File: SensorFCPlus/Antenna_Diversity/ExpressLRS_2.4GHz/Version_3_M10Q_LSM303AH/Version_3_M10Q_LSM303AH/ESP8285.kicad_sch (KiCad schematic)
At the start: 24 parts, among them U5 ESP8285H16, Y1 26MHz

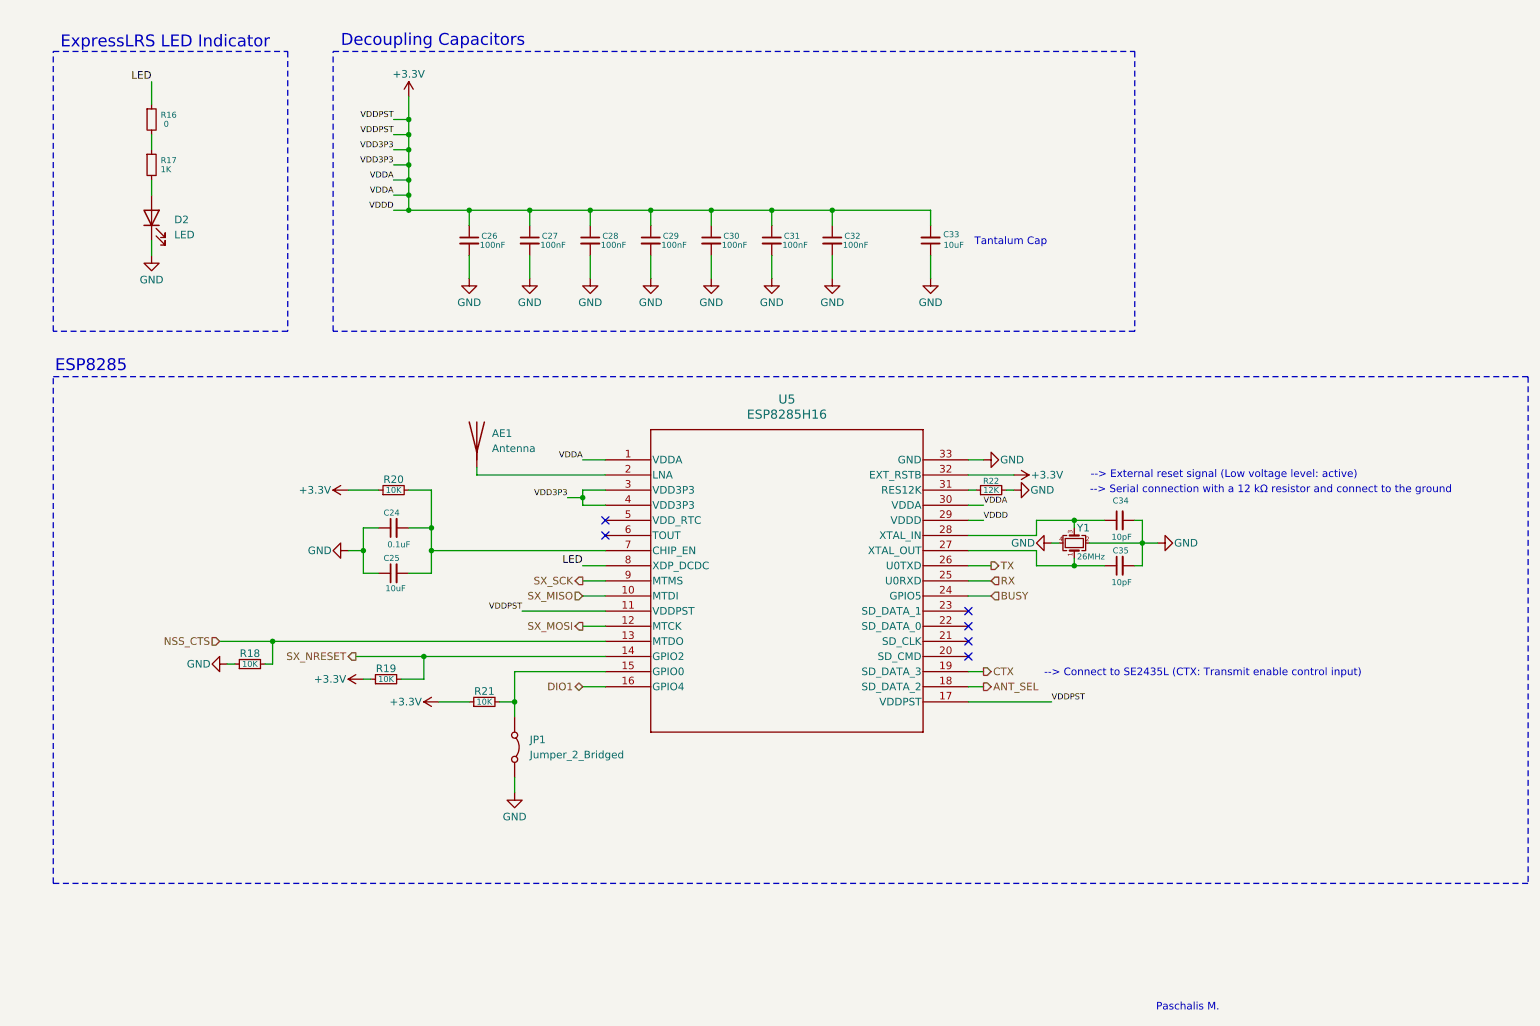
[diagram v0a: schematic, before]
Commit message: Update KiCad files for ExpressLRS modules
- Modified:
  - 2.4GHz Version 3 (M10Q LSM303AH) project and schematic files
  - 900MHz Version 3 (M10Q LSM303AH) schematic files for ESP8285 and SE2435L

- Added:
  - 2.4GHz Version 3 schematics: ESP8285, SE2431, SE2431L, SX1280
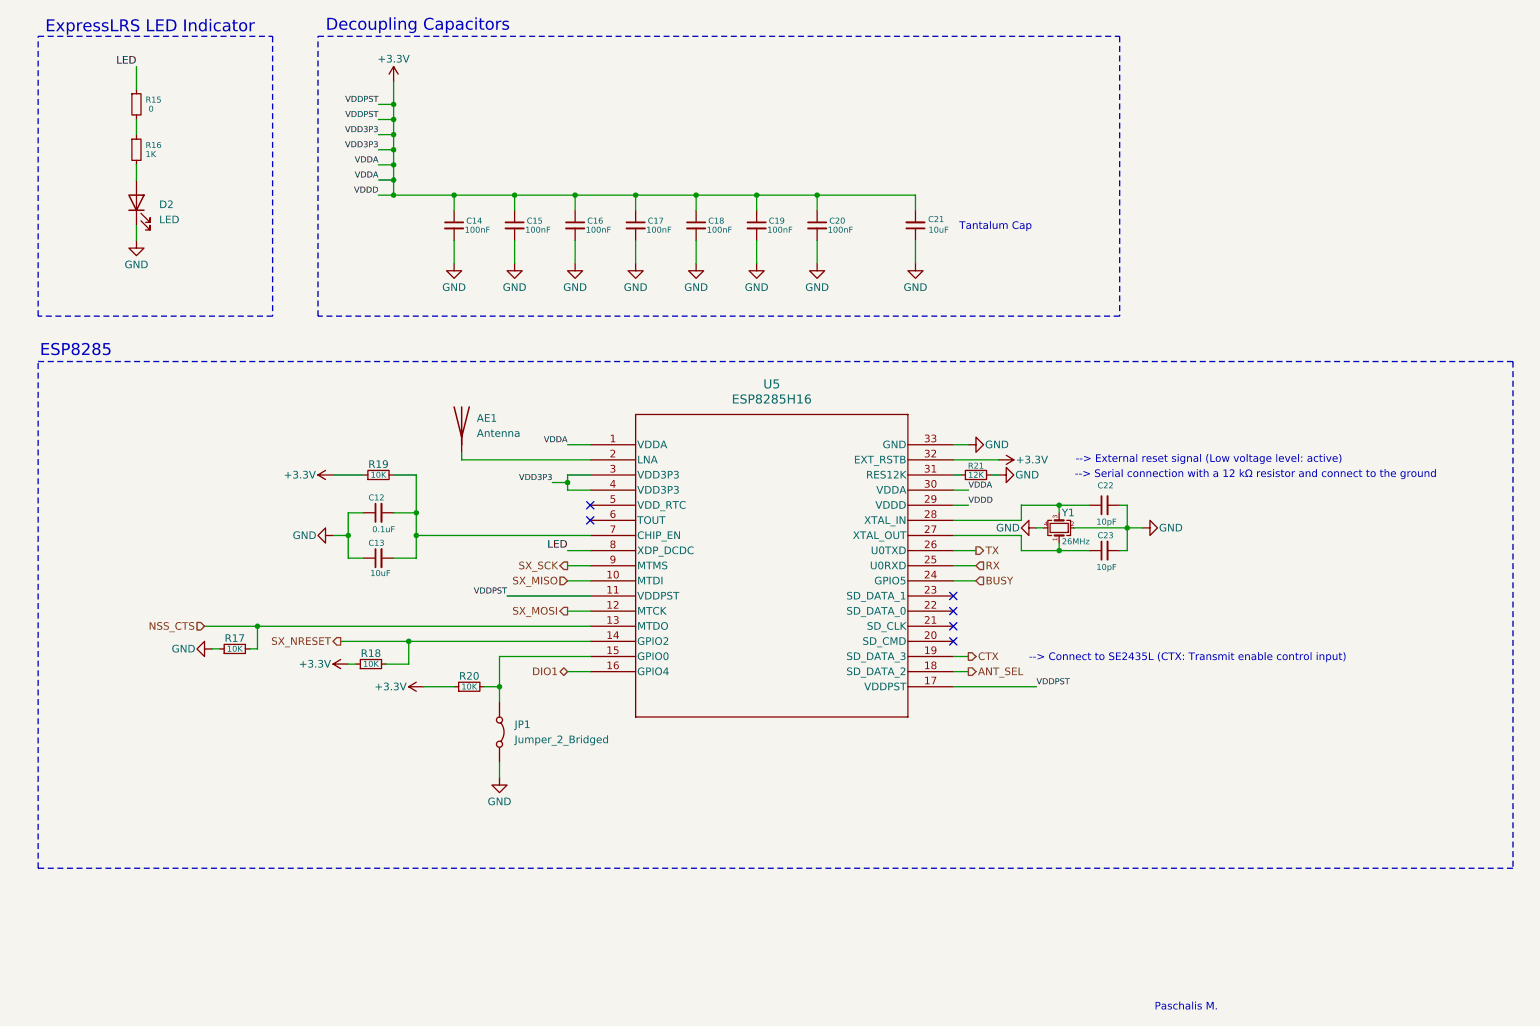
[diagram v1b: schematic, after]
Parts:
- removed C24: 0.1uF, Capacitor_SMD:C_0805_2012Metric_Pad1.18x1.45mm_HandSolder, symbol Device:C_Small
- removed C25, C33: 10uF, ECASD40J106M055K00:ECASD40J106M055K00, symbol Device:C_Small
- removed C26, C27, C28, C29, C30, C31, C32: 100nF, Capacitor_SMD:C_0805_2012Metric_Pad1.18x1.45mm_HandSolder, symbol Device:C_Small
- removed C34, C35: 10pF, Capacitor_SMD:C_0805_2012Metric_Pad1.18x1.45mm_HandSolder, symbol Device:C_Small
- removed R22: 12K, Resistor_SMD:R_0805_2012Metric_Pad1.20x1.40mm_HandSolder, symbol Device:R_Small
- added C12: 0.1uF, Capacitor_SMD:C_0805_2012Metric_Pad1.18x1.45mm_HandSolder, symbol Device:C_Small
- added C13, C21: 10uF, ECASD40J106M055K00:ECASD40J106M055K00, symbol Device:C_Small
- added C14, C15, C16, C17, C18, C19, C20: 100nF, Capacitor_SMD:C_0805_2012Metric_Pad1.18x1.45mm_HandSolder, symbol Device:C_Small
- added C22, C23: 10pF, Capacitor_SMD:C_0805_2012Metric_Pad1.18x1.45mm_HandSolder, symbol Device:C_Small
- added R15: 0, Resistor_SMD:R_0805_2012Metric_Pad1.20x1.40mm_HandSolder, symbol Device:R_Small
- R16: value 0 -> 1K
- R17: value 1K -> 10K
- R21: value 10K -> 12K
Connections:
- net +3.3V: now also R18.1, C14.1, C15.1, C16.1, C17.1, C18.1, C19.1, C20.1, C21.2; no longer R21.1
- net GND: now also R17.1, R21.2, C12.1, C13.1, C14.2, C15.2, C16.2, C17.2, C18.2, C19.2, C20.2, C21.1, C22.2, C23.2; no longer R18.1
- net LED: now also R15.1; no longer R16.1
- net NSS_CTS: now also R17.2; no longer R18.2
- net SX_NRESET: now also R18.2; no longer R19.2
- net at U5.27 (XTAL_OUT), Y1.1: now also C23.1
- net at U5.28 (XTAL_IN), Y1.3: now also C22.1
- net at JP1.1 (A), U5.15 (GPIO0): now also R20.2; no longer R21.2
- net at U5.31 (RES12K): now also R21.1
- net at U5.7 (CHIP_EN): now also R19.2, C12.2, C13.2; no longer R20.2
- net at R16.2: now also D2.2 (A); no longer R17.1
- new net: R15.2, R16.1

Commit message: Update PCB design for Version 3 M10Q LSM303AH (ESP8285, SE2431L, SX1280, and main board)
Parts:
- C12: footprint Capacitor_SMD:C_0805_2012Metric_Pad1.18x1.45mm_HandSolder -> Capacitor_SMD:C_0603_1608Metric_Pad1.08x0.95mm_HandSolder
- JP1: footprint TestPoint:TestPoint_2Pads_Pitch2.54mm_Drill0.8mm -> Jumper:SolderJumper-2_P1.3mm_Open_RoundedPad1.0x1.5mm
- R17, R18, R20, R21: footprint Resistor_SMD:R_0805_2012Metric_Pad1.20x1.40mm_HandSolder -> Resistor_SMD:R_0603_1608Metric_Pad0.98x0.95mm_HandSolder
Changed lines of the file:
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@@
 			)
 		)
-		(property "Footprint" "Resistor_SMD:R_0805_2012Metric_Pad1.20x1.40mm_HandSolder"
+		(property "Footprint" "Resistor_SMD:R_0603_1608Metric_Pad0.98x0.95mm_HandSolder"
 			(at 54.61 123.19 0)
 			(effects
@@
 			)
 		)
-		(property "Footprint" "Resistor_SMD:R_0805_2012Metric_Pad1.20x1.40mm_HandSolder"
+		(property "Footprint" "Resistor_SMD:R_0603_1608Metric_Pad0.98x0.95mm_HandSolder"
 			(at 93.98 129.54 0)
 			(effects
@@
 			)
 		)
-		(property "Footprint" "Capacitor_SMD:C_0805_2012Metric_Pad1.18x1.45mm_HandSolder"
+		(property "Footprint" "Capacitor_SMD:C_0603_1608Metric_Pad1.08x0.95mm_HandSolder"
 			(at 78.74 100.33 0)
 			(effects
@@
 			)
 		)
-		(property "Footprint" "Resistor_SMD:R_0805_2012Metric_Pad1.20x1.40mm_HandSolder"
+		(property "Footprint" "Resistor_SMD:R_0603_1608Metric_Pad0.98x0.95mm_HandSolder"
 			(at 77.47 125.73 0)
 			(effects
@@
 			)
 		)
-		(property "Footprint" "Resistor_SMD:R_0805_2012Metric_Pad1.20x1.40mm_HandSolder"
+		(property "Footprint" "Resistor_SMD:R_0603_1608Metric_Pad0.98x0.95mm_HandSolder"
 			(at 179.07 93.98 0)
 			(effects
@@
 			)
 		)
-		(property "Footprint" "TestPoint:TestPoint_2Pads_Pitch2.54mm_Drill0.8mm"
+		(property "Footprint" "Jumper:SolderJumper-2_P1.3mm_Open_RoundedPad1.0x1.5mm"
 			(at 99.06 137.16 0)
 			(effects
